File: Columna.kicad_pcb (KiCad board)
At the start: 2 copper layers, 52.5 x 222.3 mm, 72 parts, among them P1 CONN_01X21, P4 CONN_01X03

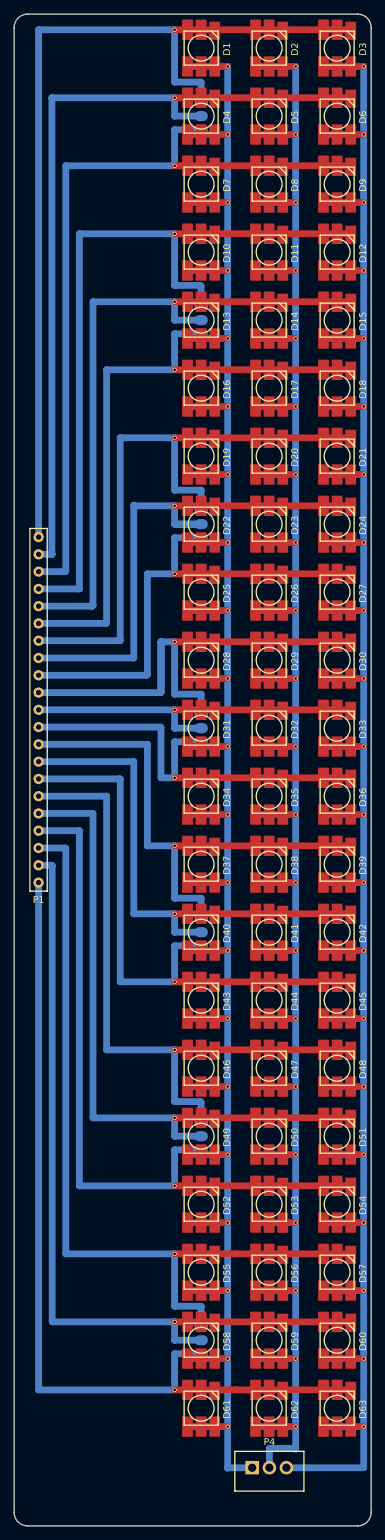
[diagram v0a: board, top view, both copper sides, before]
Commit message: Modelo 3D de los postes 1x3
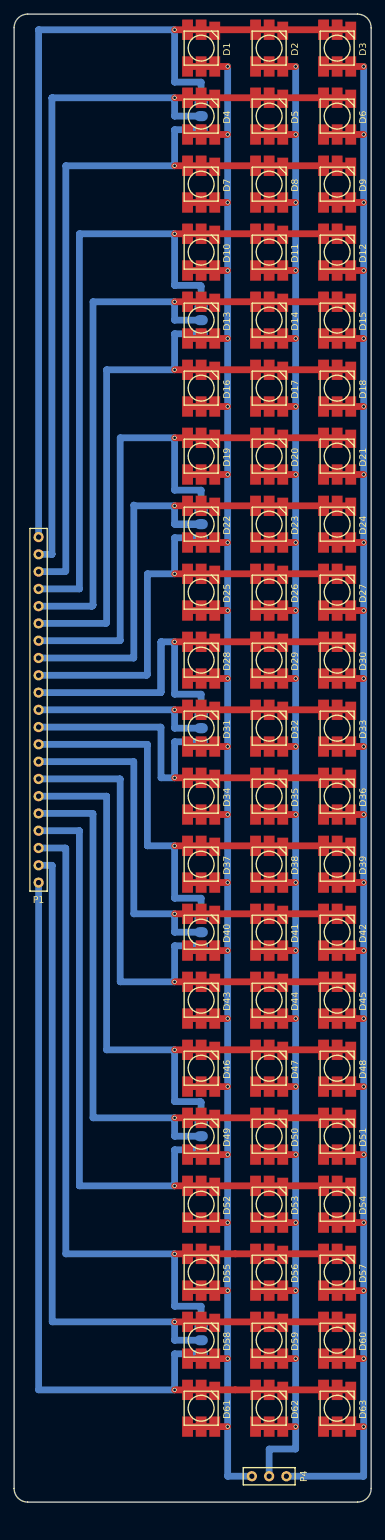
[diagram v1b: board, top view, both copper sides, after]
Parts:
- P4: footprint Connect:Wafer_Vertical10x5.8x7RM2.5-3 -> Poste:Poste_1x3
- moved P4 2.80 mm to (113.6, 239.4), turned to 90 degrees
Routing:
- net /1/K2: track 341.3 -> 342.6 mm
- net /1/K1: track 334.0 -> 335.1 mm
- net /1/K0: track 333.6 -> 334.8 mm
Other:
- board size 52.5 x 222.3 mm -> 52.5 x 218.8 mm
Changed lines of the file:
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@@
     (links 399)
     (no_connects 0)
-    (area 76.024999 24.324999 128.675001 246.775001)
+    (area 76.024999 24.324999 128.675001 243.275001)
     (thickness 1.6)
     (drawings 8)
-    (tracks 672)
+    (tracks 669)
     (zones 0)
     (modules 72)
@@
       (net 24 /7/A2))
   )
-  (module Connect:Wafer_Vertical10x5.8x7RM2.5-3 (layer F.Cu)
-    (at 111.1 238.15)
-    (descr "Gold-Tek vertical wafer connector with 2.5mm pitch")
-    (tags "wafer connector vertical")
-    (fp_text reference P4 (at 2.54 -3.81) (layer F.SilkS)
-      (effects (font (size 1 1) (thickness 0.15)))
-    )
-    (fp_text value CONN_01X03 (at 2.54 5.08) (layer F.Fab)
-      (effects (font (size 1 1) (thickness 0.15)))
-    )
-    (fp_line (start -2.75 -2.75) (end 7.85 -2.75) (layer F.CrtYd) (width 0.05))
-    (fp_line (start 7.85 -2.75) (end 7.85 3.8) (layer F.CrtYd) (width 0.05))
-    (fp_line (start 7.85 3.8) (end -2.75 3.8) (layer F.CrtYd) (width 0.05))
-    (fp_line (start -2.75 3.8) (end -2.75 -2.75) (layer F.CrtYd) (width 0.05))
-    (fp_line (start 7.62 3.429) (end -2.54 3.429) (layer F.SilkS) (width 0.15))
-    (fp_line (start -2.54 -2.413) (end 7.62 -2.413) (layer F.SilkS) (width 0.15))
-    (fp_line (start 7.62 -2.413) (end 7.62 3.429) (layer F.SilkS) (width 0.15))
-    (fp_line (start -2.54 -2.413) (end -2.54 3.429) (layer F.SilkS) (width 0.15))
-    (pad 1 thru_hole rect (at 0 0) (size 2 2) (drill 1.2) (layers *.Cu *.Mask F.SilkS)
-      (net 2 /1/K0))
-    (pad 2 thru_hole circle (at 2.54 0) (size 2 2) (drill 1.2) (layers *.Cu *.Mask F.SilkS)
-      (net 3 /1/K1))
-    (pad 3 thru_hole circle (at 5.04 0) (size 2 2) (drill 1.2) (layers *.Cu *.Mask F.SilkS)
-      (net 4 /1/K2))
-    (model Connect.3dshapes/Wafer_Vertical10x5.8x7RM2.5-3.wrl
-      (at (xyz 0 0 0))
-      (scale (xyz 4 4 4))
-      (rotate (xyz 0 0 0))
-    )
-  )
   (module Poste:Poste_1x21 (layer F.Cu)
     (at 79.7 126.7)
@@
     )
   )
-  (gr_line (start 76.1 244.7) (end 76.1 26.4) (angle 90) (layer Edge.Cuts) (width 0.15))
-  (gr_line (start 126.6 246.7) (end 78.1 246.7) (angle 90) (layer Edge.Cuts) (width 0.15))
-  (gr_line (start 128.6 26.4) (end 128.6 244.7) (angle 90) (layer Edge.Cuts) (width 0.15))
+  (module Poste:Poste_1x3 (layer F.Cu)
+    (at 113.6 239.4 90)
+    (fp_text reference P4 (at 0 5.08 90) (layer F.SilkS)
+      (effects (font (size 1 1) (thickness 0.15)))
+    )
+    (fp_text value CONN_01X03 (at 0 -5.08 90) (layer F.Fab)
+      (effects (font (size 1 1) (thickness 0.15)))
+    )
+    (fp_line (start -1.27 -3.81) (end 1.27 -3.81) (layer F.SilkS) (width 0.15))
+    (fp_line (start 1.27 -3.81) (end 1.27 3.81) (layer F.SilkS) (width 0.15))
+    (fp_line (start 1.27 3.81) (end -1.27 3.81) (layer F.SilkS) (width 0.15))
+    (fp_line (start -1.27 3.81) (end -1.27 -3.81) (layer F.SilkS) (width 0.15))
+    (pad 2 thru_hole circle (at 0 0 90) (size 1.524 1.524) (drill 0.762) (layers *.Cu *.Mask F.SilkS)
+      (net 3 /1/K1))
+    (pad 3 thru_hole circle (at 0 2.54 90) (size 1.524 1.524) (drill 0.762) (layers *.Cu *.Mask F.SilkS)
+      (net 4 /1/K2))
+    (pad 1 thru_hole circle (at 0 -2.54 90) (size 1.524 1.524) (drill 0.762) (layers *.Cu *.Mask F.SilkS)
+      (net 2 /1/K0))
+    (model ${KIPRJMOD}/3D/Poste-3D/Poste_1x3.wrl
+      (at (xyz 0 0 0))
+      (scale (xyz 0.3937 0.3937 0.3937))
+      (rotate (xyz 0 0 0))
+    )
+  )
+  (gr_line (start 78.1 243.2) (end 126.6 243.2) (layer Edge.Cuts) (width 0.15))
+  (gr_line (start 76.1 26.4) (end 76.1 241.2) (angle 90) (layer Edge.Cuts) (width 0.15))
+  (gr_line (start 128.6 241.2) (end 128.6 26.4) (angle 90) (layer Edge.Cuts) (width 0.15))
+  (gr_arc (start 78.1 241.2) (end 78.1 243.2) (angle 90) (layer Edge.Cuts) (width 0.15))
+  (gr_arc (start 126.6 241.2) (end 128.6 241.2) (angle 90) (layer Edge.Cuts) (width 0.15))
   (gr_line (start 78.1 24.4) (end 126.6 24.4) (angle 90) (layer Edge.Cuts) (width 0.15))
-  (gr_arc (start 126.6 244.7) (end 128.6 244.7) (angle 90) (layer Edge.Cuts) (width 0.15))
-  (gr_arc (start 78.1 244.7) (end 78.1 246.7) (angle 90) (layer Edge.Cuts) (width 0.15))
   (gr_arc (start 78.1 26.4) (end 76.1 26.4) (angle 90) (layer Edge.Cuts) (width 0.15))
   (gr_arc (start 126.6 26.4) (end 126.6 24.4) (angle 90) (layer Edge.Cuts) (width 0.15))
@@
   (segment (start 121.6 26.7) (end 123.6 26.7) (width 1) (layer F.Cu) (net 1))
   (segment (start 123.6 26.7) (end 125.6 26.7) (width 1) (layer F.Cu) (net 1))
-  (segment (start 107.5 232.1) (end 107.5 238.2) (width 1) (layer B.Cu) (net 2))
-  (segment (start 107.55 238.15) (end 111.1 238.15) (width 1) (layer B.Cu) (net 2))
-  (segment (start 107.5 238.2) (end 107.55 238.15) (width 1) (layer B.Cu) (net 2))
+  (segment (start 107.5 239.4) (end 111.06 239.4) (width 1) (layer B.Cu) (net 2))
+  (segment (start 107.5 232.1) (end 107.5 239.4) (width 1) (layer B.Cu) (net 2))
   (segment (start 105.6 222.1) (end 107.5 222.1) (width 1) (layer F.Cu) (net 2))
   (via (at 107.5 222.1) (size 0.6) (drill 0.4) (layers F.Cu B.Cu) (net 2))
@@
   (segment (start 107.5 32.1) (end 107.5 42.1) (width 1) (layer B.Cu) (net 2))
   (segment (start 107.5 232.1) (end 105.6 232.1) (width 1) (layer F.Cu) (net 2))
-  (via (at 107.5 232.1) (size 0.6) (drill 0.4) (layers F.Cu B.Cu) (net 2))
   (segment (start 107.5 52.1) (end 107.5 62.1) (width 1) (layer B.Cu) (net 2))
   (segment (start 107.5 62.1) (end 107.5 72.1) (width 1) (layer B.Cu) (net 2))
@@
   (segment (start 107.5 202.1) (end 107.5 212.1) (width 1) (layer B.Cu) (net 2))
   (segment (start 107.5 212.1) (end 107.5 222.1) (width 1) (layer B.Cu) (net 2))
-  (segment (start 107.5 222.1) (end 107.5 232.1) (width 1) (layer B.Cu) (net 2))
   (segment (start 107.5 42.1) (end 107.5 52.1) (width 1) (layer B.Cu) (net 2))
   (segment (start 101.6 232.1) (end 103.6 232.1) (width 1) (layer F.Cu) (net 2))
@@
   (segment (start 101.6 32.1) (end 103.6 32.1) (width 1) (layer F.Cu) (net 2))
   (segment (start 103.6 32.1) (end 105.6 32.1) (width 1) (layer F.Cu) (net 2))
-  (segment (start 117.5 232.1) (end 117.5 235.4) (width 1) (layer B.Cu) (net 3))
-  (segment (start 117.4 235.3) (end 113.64 235.3) (width 1) (layer B.Cu) (net 3))
-  (segment (start 117.5 235.4) (end 117.4 235.3) (width 1) (layer B.Cu) (net 3))
+  (via (at 107.5 232.1) (size 0.6) (drill 0.4) (layers F.Cu B.Cu) (net 2))
+  (segment (start 107.5 222.1) (end 107.5 232.1) (width 1) (layer B.Cu) (net 2))
+  (segment (start 113.6 235.4) (end 117.5 235.4) (width 1) (layer B.Cu) (net 3))
+  (segment (start 113.6 239.4) (end 113.6 235.4) (width 1) (layer B.Cu) (net 3))
+  (segment (start 117.5 235.4) (end 117.5 232.1) (width 1) (layer B.Cu) (net 3))
   (segment (start 115.6 222.1) (end 117.5 222.1) (width 1) (layer F.Cu) (net 3))
   (via (at 117.5 222.1) (size 0.6) (drill 0.4) (layers F.Cu B.Cu) (net 3))
@@
   (segment (start 115.6 42.1) (end 117.5 42.1) (width 1) (layer F.Cu) (net 3))
   (via (at 117.5 42.1) (size 0.6) (drill 0.4) (layers F.Cu B.Cu) (net 3))
-  (segment (start 113.64 235.3) (end 113.64 238.15) (width 1) (layer B.Cu) (net 3))
   (segment (start 115.6 232.1) (end 117.5 232.1) (width 1) (layer F.Cu) (net 3))
   (segment (start 117.5 32.1) (end 115.6 32.1) (width 1) (layer F.Cu) (net 3))
@@
   (segment (start 113.6 32.1) (end 115.6 32.1) (width 1) (layer F.Cu) (net 3))
   (segment (start 111.6 32.1) (end 113.6 32.1) (width 1) (layer F.Cu) (net 3))
-  (segment (start 116.14 238.15) (end 127.45 238.15) (width 1) (layer B.Cu) (net 4))
-  (segment (start 127.5 238.1) (end 127.5 232.1) (width 1) (layer B.Cu) (net 4))
-  (segment (start 127.45 238.15) (end 127.5 238.1) (width 1) (layer B.Cu) (net 4))
+  (segment (start 127.5 239.4) (end 127.5 232.1) (width 1) (layer B.Cu) (net 4))
+  (segment (start 116.14 239.4) (end 127.5 239.4) (width 1) (layer B.Cu) (net 4))
   (segment (start 125.6 222.1) (end 127.5 222.1) (width 1) (layer F.Cu) (net 4))
   (via (at 127.5 222.1) (size 0.6) (drill 0.4) (layers F.Cu B.Cu) (net 4))
@@
   (segment (start 123.6 86.7) (end 125.6 86.7) (width 1) (layer F.Cu) (net 10))
   (segment (start 99.7 96.7) (end 93.8 96.7) (width 1) (layer B.Cu) (net 11))
-  (segment (start 93.8 96.7) (end 93.7 96.6) (width 1) (layer B.Cu) (net 11))
-  (segment (start 93.68 119.08) (end 93.7 119.06) (width 1) (layer B.Cu) (net 11))
-  (segment (start 93.7 119.06) (end 93.7 96.6) (width 1) (layer B.Cu) (net 11))
   (segment (start 93.68 119.08) (end 79.7 119.08) (width 1) (layer B.Cu) (net 11))
+  (segment (start 93.7 119.06) (end 93.7 96.6) (width 1) (layer B.Cu) (net 11))
+  (segment (start 93.68 119.08) (end 93.7 119.06) (width 1) (layer B.Cu) (net 11))
+  (segment (start 93.8 96.7) (end 93.7 96.6) (width 1) (layer B.Cu) (net 11))
   (segment (start 99.7 96.7) (end 99.7 99.4) (width 1) (layer B.Cu) (net 11))
   (segment (start 99.7 99.4) (end 103.6 99.4) (width 1) (layer B.Cu) (net 11))
@@
   (segment (start 123.6 216.7) (end 125.6 216.7) (width 1) (layer F.Cu) (net 23))
   (segment (start 99.7 226.7) (end 79.7 226.7) (width 1) (layer B.Cu) (net 24))
+  (via (at 99.7 226.7) (size 0.6) (drill 0.4) (layers F.Cu B.Cu) (net 24))
+  (segment (start 99.7 221.4) (end 99.7 226.7) (width 1) (layer B.Cu) (net 24))
   (segment (start 79.7 226.7) (end 79.7 152.1) (width 1) (layer B.Cu) (net 24))
   (segment (start 103.6 221.4) (end 99.7 221.4) (width 1) (layer B.Cu) (net 24))
   (segment (start 99.7 226.7) (end 101.6 226.7) (width 1) (layer F.Cu) (net 24))
-  (via (at 99.7 226.7) (size 0.6) (drill 0.4) (layers F.Cu B.Cu) (net 24))
-  (segment (start 99.7 221.4) (end 99.7 226.7) (width 1) (layer B.Cu) (net 24))
   (segment (start 101.6 226.7) (end 103.6 226.7) (width 1) (layer F.Cu) (net 24))
   (segment (start 103.6 226.7) (end 105.6 226.7) (width 1) (layer F.Cu) (net 24))
